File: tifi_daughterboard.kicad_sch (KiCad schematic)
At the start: 19 parts, among them J1 SSW-110-23-F-D, J2 SSW-110-23-F-D, J3 SM04B-SRSS-TB(LF)(SN), J4 SSW-103-02-T-S-RA, Q1 BSS138LT1G, U1 SGP40-D-R4, U2 SHT40-AD1B-R3

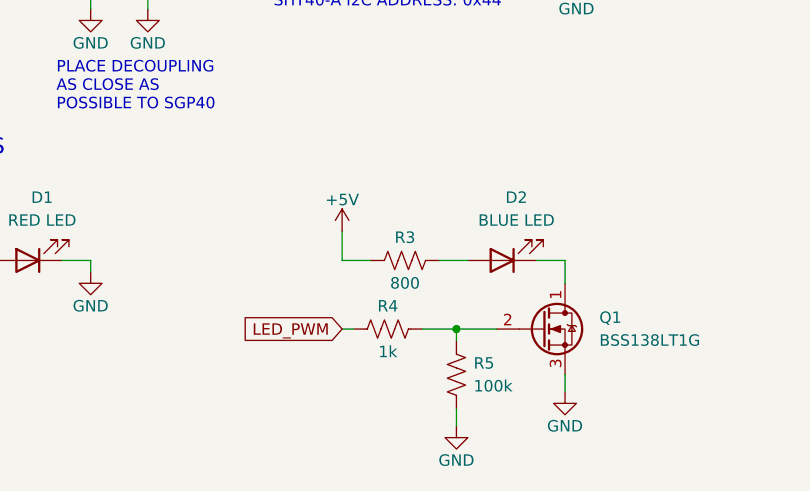
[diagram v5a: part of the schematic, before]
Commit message: Assign footprints to discrete components.
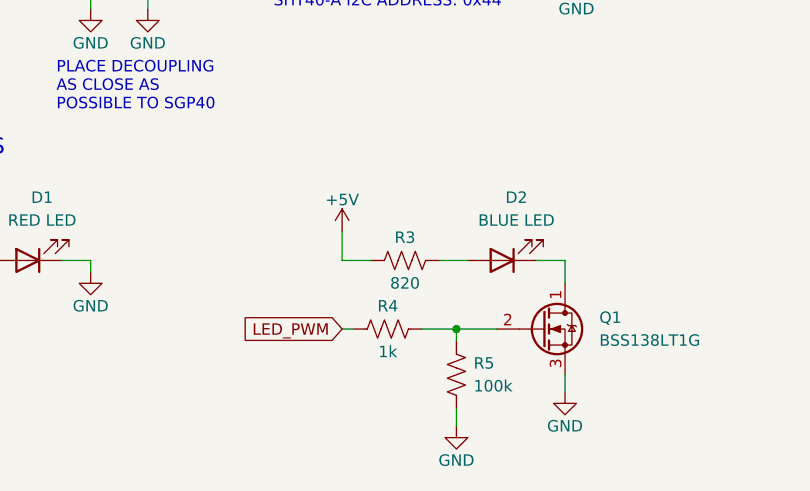
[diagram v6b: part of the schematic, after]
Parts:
- C1, C2: footprint (none) -> Capacitor_SMD:C_0805_2012Metric
- Q1: footprint (none) -> Package_TO_SOT_SMD:SOT-23W
- R1, R2, R4, R5, R6: footprint (none) -> Resistor_SMD:R_0805_2012Metric
- R3: value 800 -> 820; footprint (none) -> Resistor_SMD:R_0805_2012Metric
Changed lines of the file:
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@@
       (effects (font (size 1.27 1.27)) (justify left))
     )
-    (property "Footprint" "" (id 2) (at 150.1902 46.355 0)
+    (property "Footprint" "Capacitor_SMD:C_0805_2012Metric" (id 2) (at 150.1902 46.355 0)
       (effects (font (size 1.27 1.27)) hide)
     )
@@
       (effects (font (size 1.27 1.27)) (justify left))
     )
-    (property "Footprint" "" (id 2) (at 184.531 88.519 90)
+    (property "Footprint" "Resistor_SMD:R_0805_2012Metric" (id 2) (at 184.531 88.519 90)
       (effects (font (size 1.27 1.27)) hide)
     )
@@
     (in_bom yes) (on_board yes)
     (property "Reference" "R3" (id 0) (at 177.8 73.025 90))
-    (property "Value" "800" (id 1) (at 177.8 78.105 90))
-    (property "Footprint" "" (id 2) (at 178.054 74.549 90)
+    (property "Value" "820" (id 1) (at 177.8 78.105 90))
+    (property "Footprint" "Resistor_SMD:R_0805_2012Metric" (id 2) (at 178.054 74.549 90)
       (effects (font (size 1.27 1.27)) hide)
     )
@@
       (effects (font (size 1.27 1.27)) (justify left))
     )
-    (property "Footprint" "" (id 2) (at 150.241 32.639 90)
+    (property "Footprint" "Resistor_SMD:R_0805_2012Metric" (id 2) (at 150.241 32.639 90)
       (effects (font (size 1.27 1.27)) hide)
     )
@@
       (effects (font (size 1.27 1.27)) (justify left))
     )
-    (property "Footprint" "" (id 2) (at 241.046 30.734 90)
+    (property "Footprint" "Resistor_SMD:R_0805_2012Metric" (id 2) (at 241.046 30.734 90)
       (effects (font (size 1.27 1.27)) hide)
     )
@@
     (property "Reference" "R4" (id 0) (at 175.895 80.645 90))
     (property "Value" "1k" (id 1) (at 175.895 85.725 90))
-    (property "Footprint" "" (id 2) (at 176.149 82.169 90)
+    (property "Footprint" "Resistor_SMD:R_0805_2012Metric" (id 2) (at 176.149 82.169 90)
       (effects (font (size 1.27 1.27)) hide)
     )
@@
       (effects (font (size 1.27 1.27)) (justify left))
     )
-    (property "Footprint" "" (id 2) (at 198.12 80.645 0)
+    (property "Footprint" "Package_TO_SOT_SMD:SOT-23W" (id 2) (at 198.12 80.645 0)
       (effects (font (size 1.27 1.27)) hide)
     )
@@
   (symbol (lib_id "power:PWR_FLAG") (at 95.25 29.21 0) (unit 1)
     (in_bom yes) (on_board yes)
-    (property "Reference" "#FLG?" (id 0) (at 95.25 27.305 0)
+    (property "Reference" "#FLG0102" (id 0) (at 95.25 27.305 0)
       (effects (font (size 1.27 1.27)) hide)
     )
@@
       (effects (font (size 1.27 1.27)) (justify right))
     )
-    (property "Footprint" "" (id 2) (at 117.8052 40.005 0)
+    (property "Footprint" "Capacitor_SMD:C_0805_2012Metric" (id 2) (at 117.8052 40.005 0)
       (effects (font (size 1.27 1.27)) hide)
     )
@@
     (property "Reference" "R1" (id 0) (at 125.73 69.85 90))
     (property "Value" "330" (id 1) (at 125.73 72.39 90))
-    (property "Footprint" "" (id 2) (at 125.984 74.549 90)
+    (property "Footprint" "Resistor_SMD:R_0805_2012Metric" (id 2) (at 125.984 74.549 90)
       (effects (font (size 1.27 1.27)) hide)
     )
@@
     )
     (path "/b3927d09-352f-4ec4-bda6-e34d462de82c"
-      (reference "#FLG?") (unit 1) (value "PWR_FLAG") (footprint "")
+      (reference "#FLG0102") (unit 1) (value "PWR_FLAG") (footprint "")
     )
     (path "/7d97e865-7860-4bff-9e38-c39efb9297b4"
@@
     )
     (path "/ea0ce901-a5ee-433c-8170-870cbb35faf2"
-      (reference "C1") (unit 1) (value "1uF") (footprint "")
+      (reference "C1") (unit 1) (value "1uF") (footprint "Capacitor_SMD:C_0805_2012Metric")
     )
     (path "/40d41fd6-b6a8-45bf-9e03-7d7bb2b06a12"
-      (reference "C2") (unit 1) (value "1uF") (footprint "")
+      (reference "C2") (unit 1) (value "1uF") (footprint "Capacitor_SMD:C_0805_2012Metric")
     )
     (path "/2c04621a-bbf8-472b-bd15-1b74530f6f21"
@@
     )
     (path "/a693ce77-e4fb-4d3a-afc5-f19cee5f74f8"
-      (reference "Q1") (unit 1) (value "BSS138LT1G") (footprint "")
+      (reference "Q1") (unit 1) (value "BSS138LT1G") (footprint "Package_TO_SOT_SMD:SOT-23W")
     )
     (path "/f1ede1c9-4507-494d-9d3c-c58508b0d150"
-      (reference "R1") (unit 1) (value "330") (footprint "")
+      (reference "R1") (unit 1) (value "330") (footprint "Resistor_SMD:R_0805_2012Metric")
     )
     (path "/71672d3b-4690-4212-bfa4-42f5ad120dbb"
-      (reference "R2") (unit 1) (value "4.7") (footprint "")
+      (reference "R2") (unit 1) (value "4.7") (footprint "Resistor_SMD:R_0805_2012Metric")
     )
     (path "/6ead0172-9da0-4bb9-b4f7-c2813d5d4f9a"
-      (reference "R3") (unit 1) (value "800") (footprint "")
+      (reference "R3") (unit 1) (value "820") (footprint "Resistor_SMD:R_0805_2012Metric")
     )
     (path "/a35e02c9-d012-486b-b944-b7a878963770"
-      (reference "R4") (unit 1) (value "1k") (footprint "")
+      (reference "R4") (unit 1) (value "1k") (footprint "Resistor_SMD:R_0805_2012Metric")
     )
     (path "/6bb9cb59-0088-470e-a1b1-51abbe6783ad"
-      (reference "R5") (unit 1) (value "100k") (footprint "")
+      (reference "R5") (unit 1) (value "100k") (footprint "Resistor_SMD:R_0805_2012Metric")
     )
     (path "/9c308a55-9b41-494b-8e37-68974a4c9bd3"
-      (reference "R6") (unit 1) (value "10k") (footprint "")
+      (reference "R6") (unit 1) (value "10k") (footprint "Resistor_SMD:R_0805_2012Metric")
     )
     (path "/f5356d0d-ea25-437c-9f9a-3a02cfee54ec"

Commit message: Add SHT40 SnapEDA model. Assign footprint.
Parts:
- U1: footprint (none) -> TiFi Footprints:DFN-6-1EP_2.44x2.44mm_P0.8mm_EP1.25x1.7mm
- U2: footprint (none) -> SHT40:XDCR_SHT40-AD1B-R2
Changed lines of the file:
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@@
     (property "Reference" "U1" (id 0) (at 128.905 34.29 0))
     (property "Value" "SGP40-D-R4" (id 1) (at 133.985 45.72 0))
-    (property "Footprint" "" (id 2) (at 125.73 37.465 0)
+    (property "Footprint" "TiFi Footprints:DFN-6-1EP_2.44x2.44mm_P0.8mm_EP1.25x1.7mm" (id 2) (at 125.73 37.465 0)
       (effects (font (size 1.27 1.27)) hide)
     )
@@
     (property "Reference" "U2" (id 0) (at 180.975 33.655 0))
     (property "Value" "SHT40-AD1B-R3" (id 1) (at 185.42 43.18 0))
-    (property "Footprint" "" (id 2) (at 177.8 36.83 0)
+    (property "Footprint" "SHT40:XDCR_SHT40-AD1B-R2" (id 2) (at 177.8 36.83 0)
       (effects (font (size 1.27 1.27)) hide)
     )
@@
     )
     (path "/0d00eb67-db68-470c-ac62-866cefaa8448"
-      (reference "U1") (unit 1) (value "SGP40-D-R4") (footprint "")
+      (reference "U1") (unit 1) (value "SGP40-D-R4") (footprint "TiFi Footprints:DFN-6-1EP_2.44x2.44mm_P0.8mm_EP1.25x1.7mm")
     )
     (path "/26e53336-a088-483e-9566-abc27c489b08"
-      (reference "U2") (unit 1) (value "SHT40-AD1B-R3") (footprint "")
-    )
-  )
+      (reference "U2") (unit 1) (value "SHT40-AD1B-R3") (footprint "SHT40:XDCR_SHT40-AD1B-R2")
+    )
+  )

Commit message: Rough layout draft.
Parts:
- C3: footprint (none) -> Capacitor_SMD:C_0805_2012Metric
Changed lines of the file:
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@@
       (effects (font (size 1.27 1.27)) (justify left))
     )
-    (property "Footprint" "" (id 2) (at 202.2602 41.91 0)
+    (property "Footprint" "Capacitor_SMD:C_0805_2012Metric" (id 2) (at 202.2602 41.91 0)
       (effects (font (size 1.27 1.27)) hide)
     )
@@
     )
     (path "/2c04621a-bbf8-472b-bd15-1b74530f6f21"
-      (reference "C3") (unit 1) (value "100nF") (footprint "")
+      (reference "C3") (unit 1) (value "100nF") (footprint "Capacitor_SMD:C_0805_2012Metric")
     )
     (path "/c6c05906-684a-4ea4-8501-9bf3dd4b9c99"
